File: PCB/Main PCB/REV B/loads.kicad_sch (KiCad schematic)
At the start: 27 parts, among them Q3 2N7002, Q4 2N7002, Q5 2N7002, U10 TLP2362TPR_E, U11 ALDP105W, U12 TLP2362TPR_E, U13 ALDP105W, U8 ALDP105W, U9 TLP2362TPR_E

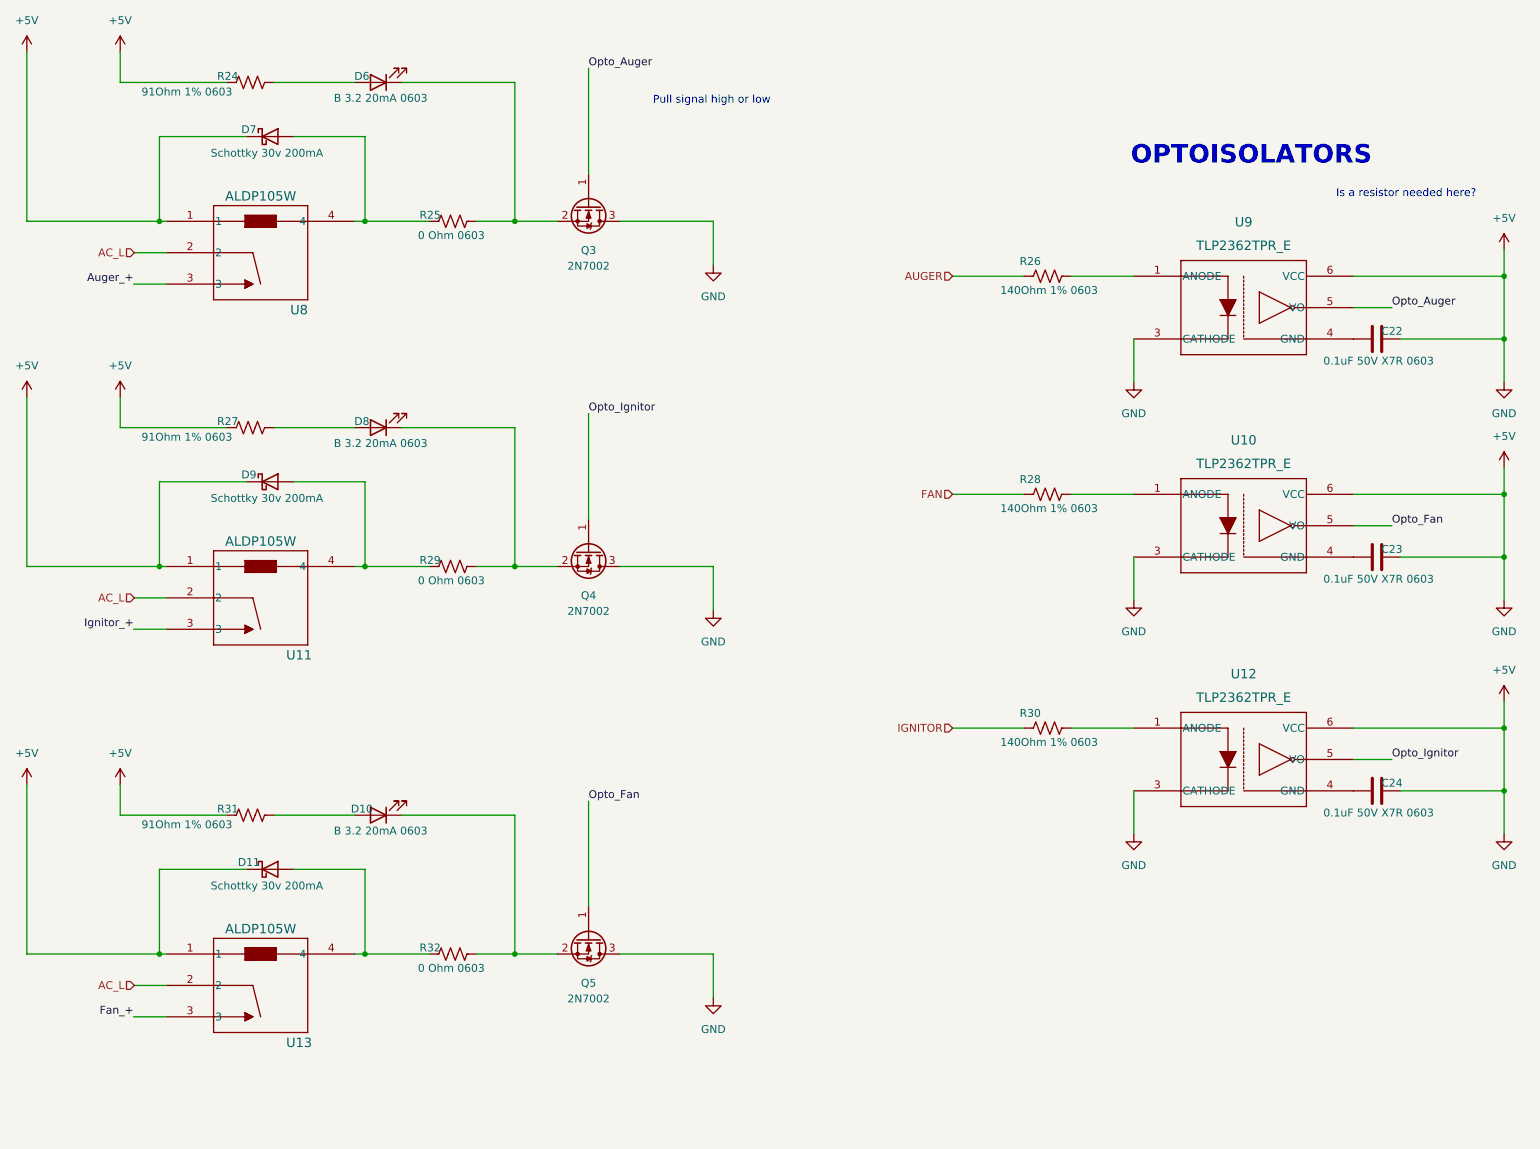
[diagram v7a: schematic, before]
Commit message: PCB schematic updates, Reboot circuit fixed
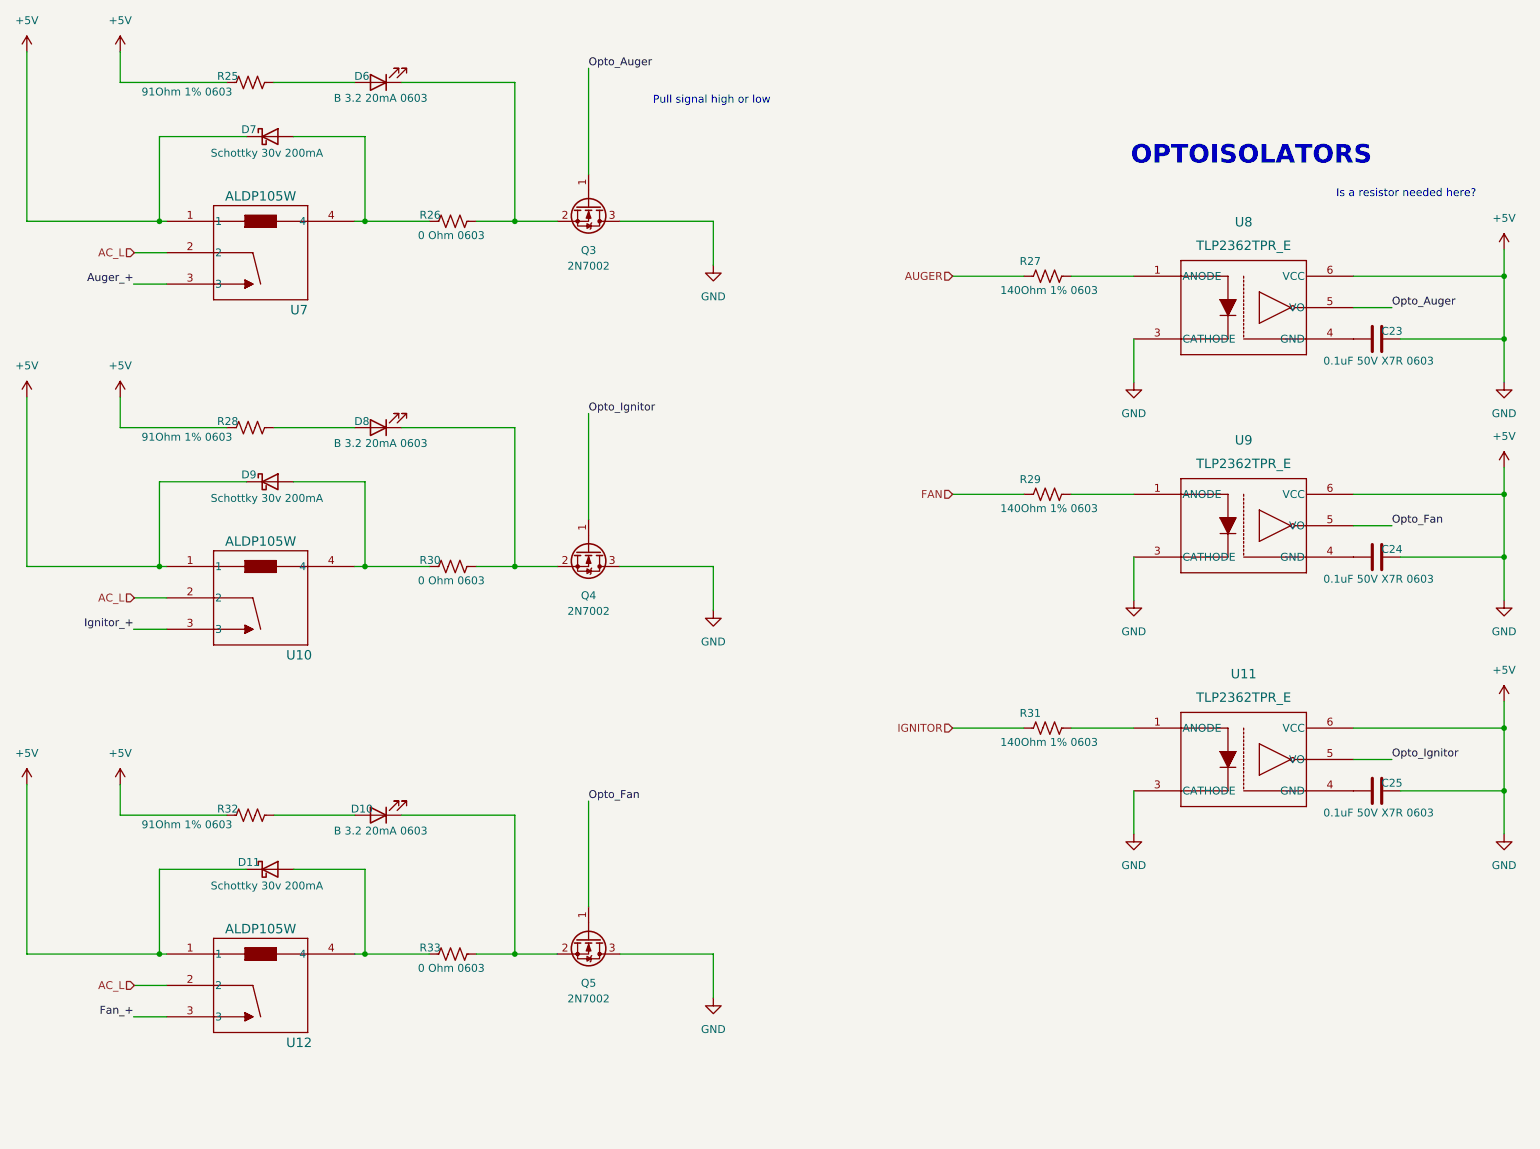
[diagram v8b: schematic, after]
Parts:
- renumbered C22 to C23, C23 to C24, C24 to C25, R24 to R25, R25 to R26, R26 to R27, R27 to R28, R28 to R29, R29 to R30, R30 to R31, R31 to R32, R32 to R33, U11 to U10, U12 to U11, U13 to U12, U8 to U7, U9 to U8, U10 to U9
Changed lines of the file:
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@@
 (kicad_sch (version 20211123) (generator eeschema)
-  (paper "A4")
+  (paper "A2")
